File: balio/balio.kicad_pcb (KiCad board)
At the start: 2 copper layers, 280 x 60 mm, 69 parts, among them J1 IN1, J10 OUT4, J11 OUT3, J12 OUT4, J13 MON3, J14 MON4, J15 MON3, J16 MON4, J17 POWER, J18 POWER, J2 IN2, J3 IN1, J4 IN2, J5 OUT1, J6 OUT2, J7 IN3, J8 IN4, J9 OUT3, U1 INA134, U2 INA134, U3 TL072, U4 TL072

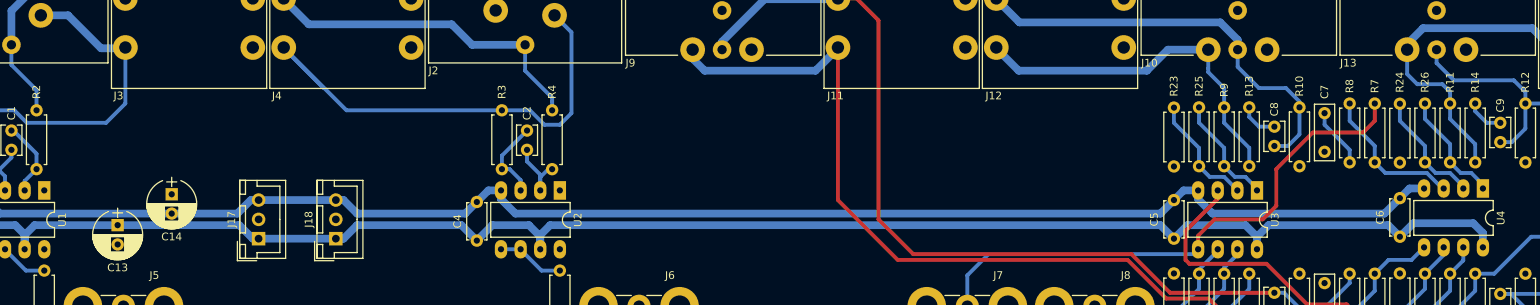
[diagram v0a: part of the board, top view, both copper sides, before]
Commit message: Upgrade balio to Kicad 6
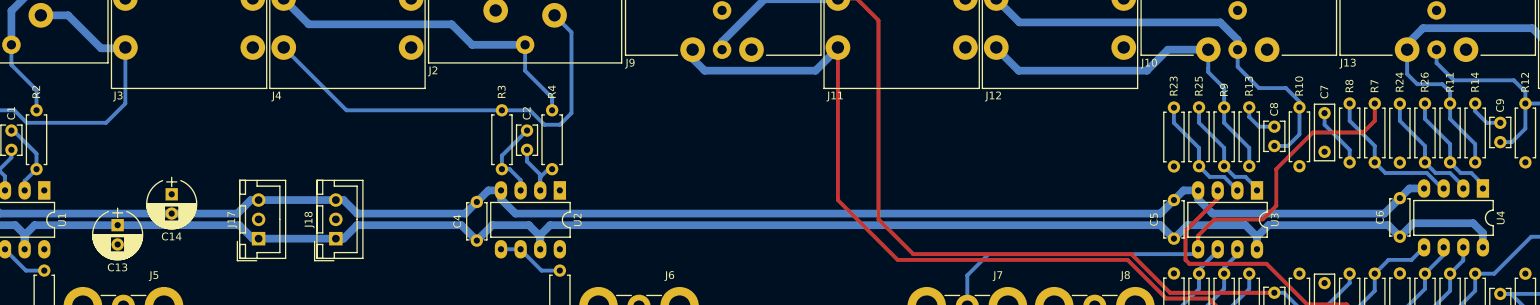
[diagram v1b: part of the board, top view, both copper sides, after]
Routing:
- net Net-(J2-Pad2): track 62.9 -> 55.6 mm
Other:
- net class Default removed
- net class Power removed
